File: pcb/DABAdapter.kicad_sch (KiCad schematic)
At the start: 39 parts, among them J1 RFShield_OnePiece, J2 Ant, J3 Conn_01x06, J4 AudioJack3_Ground, J6 Conn_01x06, U3 abcdefg, U4 MIC5504-1.8YM5, Y1 19.2Mhz

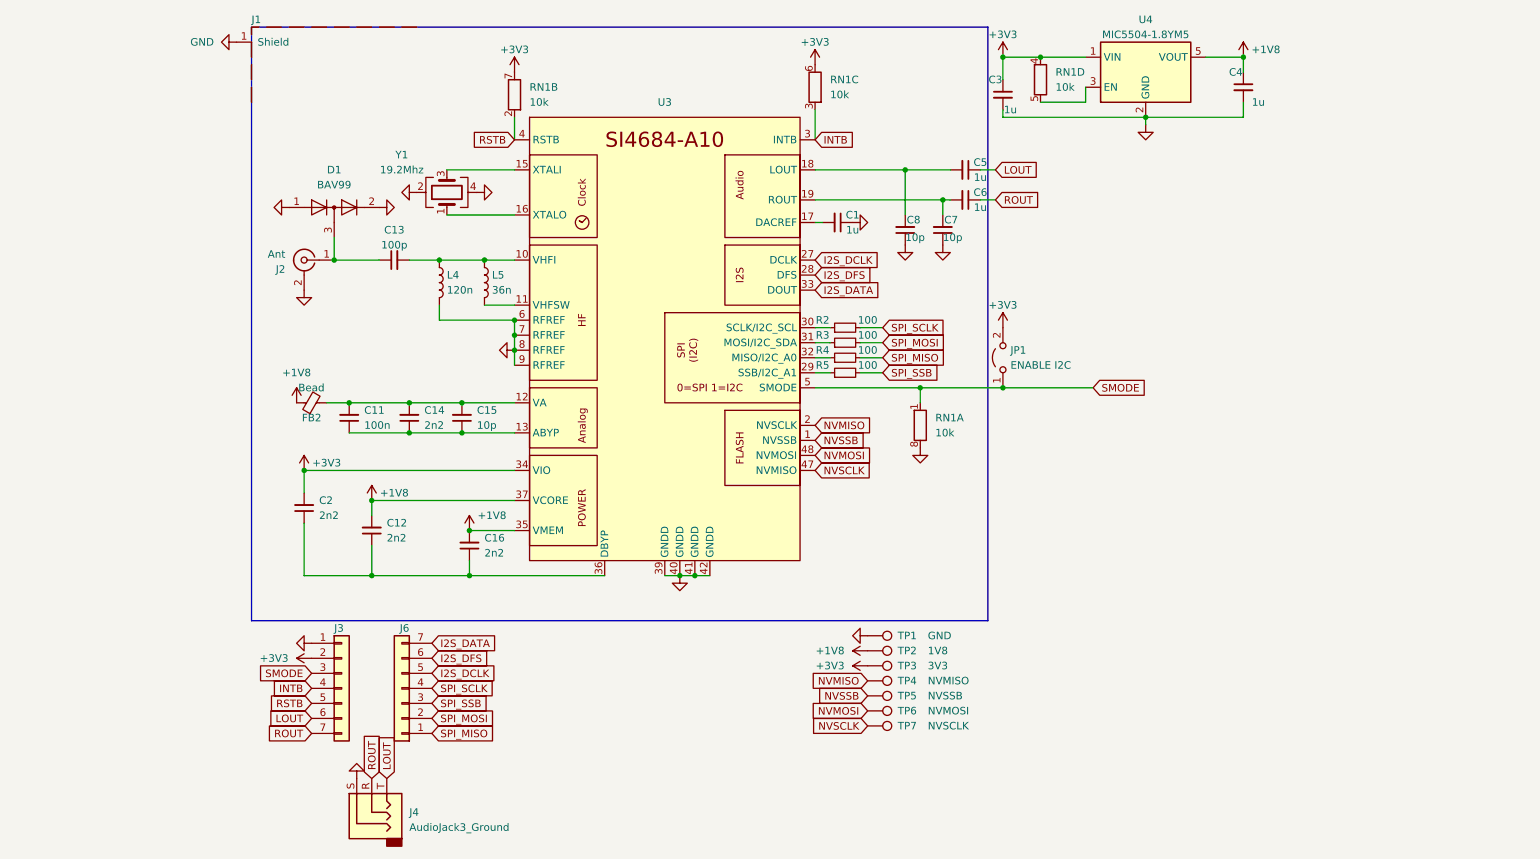
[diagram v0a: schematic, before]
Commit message: Add flash chip to the layout
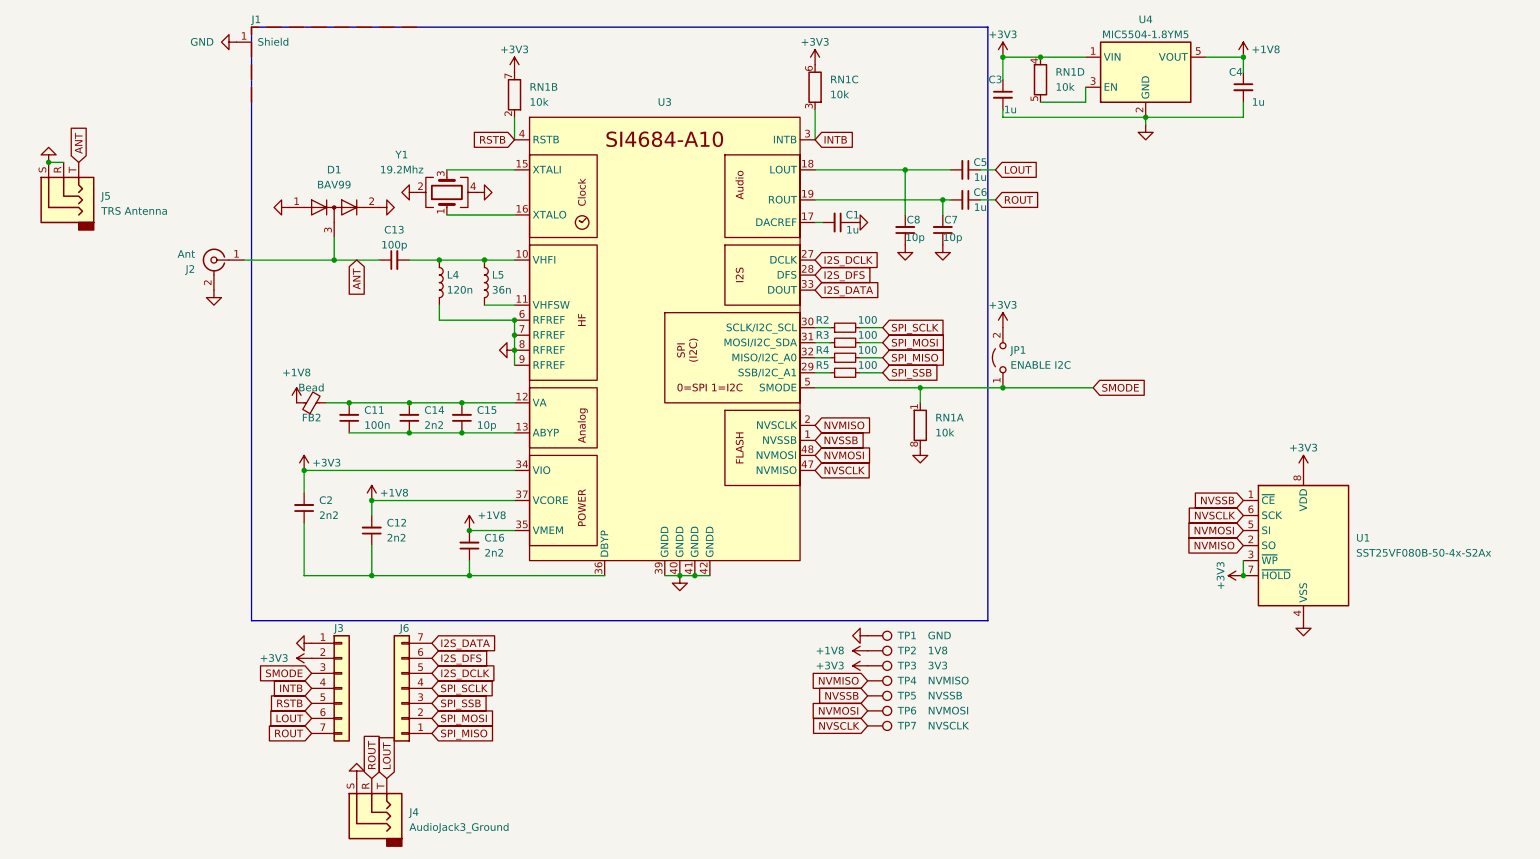
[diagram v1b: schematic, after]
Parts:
- added J5: TRS Antenna, Connector_Audio:Jack_3.5mm_CUI_SJ-3523-SMT_Horizontal, symbol Connector_Audio:AudioJack3
- added U1: SST25VF080B-50-4x-S2Ax, Package_SO:SOIC-8_5.275x5.275mm_P1.27mm, symbol Memory_Flash:SST25VF080B-50-4x-S2Ax
- C15, C7, C8: footprint jlc_footprints:C0603 -> jlc_footprints:C0402
- U3: LCSC (none) -> C2654613
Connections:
- net +3V3: now also U1.3 (~{WP}), U1.7 (~{HOLD}), U1.8 (VDD)
- net GND: now also J5.R, J5.S, U1.4 (VSS)
- net NVMISO: now also U1.2 (SO)
- net NVMOSI: now also U1.5 (SI)
- net NVSCLK: now also U1.6 (SCK)
- net NVSSB: now also U1.1 (~{CE})
- net ANT: now reaches C13.1, D1.3 (K), J2.1 (In)
- net ANT: now also J5.T
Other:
- moved on the sheet: J2

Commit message: Routing of the pcb
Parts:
- removed J5: TRS Antenna, Connector_Audio:Jack_3.5mm_CUI_SJ-3523-SMT_Horizontal, symbol Connector_Audio:AudioJack3
- removed JP1: ENABLE I2C, symbol Jumper:Jumper_2_Open
- removed RN1: 10k, jlc_footprints:RES-ARRAY-SMD_0603-8P-L3.2-W1.6-BL, symbol Device:R_Network04_Split
- added R1, R6, R7, R8: 10k, jlc_footprints:C0402, symbol Device:R_Small
- U1: now not fitted
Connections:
- net +3V3: now also R1.1, R6.1, R7.1
- net GND: now also R8.2
- net I2S_DCLK: now also J6.6 (Pin_6); no longer J6.5 (Pin_5)
- net I2S_DFS: now also J6.5 (Pin_5); no longer J6.6 (Pin_6)
- net INTB: now also J3.5 (Pin_5), R6.2; no longer J3.4 (Pin_4)
- net LOUT: now also J3.4 (Pin_4); no longer J3.6 (Pin_6)
- net ROUT: now also J3.3 (Pin_3); no longer J3.7 (Pin_7)
- net RSTB: now also J3.6 (Pin_6), R7.2; no longer J3.5 (Pin_5)
- net SMODE: now also J3.7 (Pin_7), R8.1; no longer J3.3 (Pin_3)
- net SPI_SCLK: now also J6.3 (Pin_3); no longer J6.4 (Pin_4)
- net SPI_SSB: now also J6.4 (Pin_4); no longer J6.3 (Pin_3)
- net at U4.3 (EN): now also R1.2
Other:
- moved on the sheet: C3, C4, J6, R2, R3, R4, R5, U4

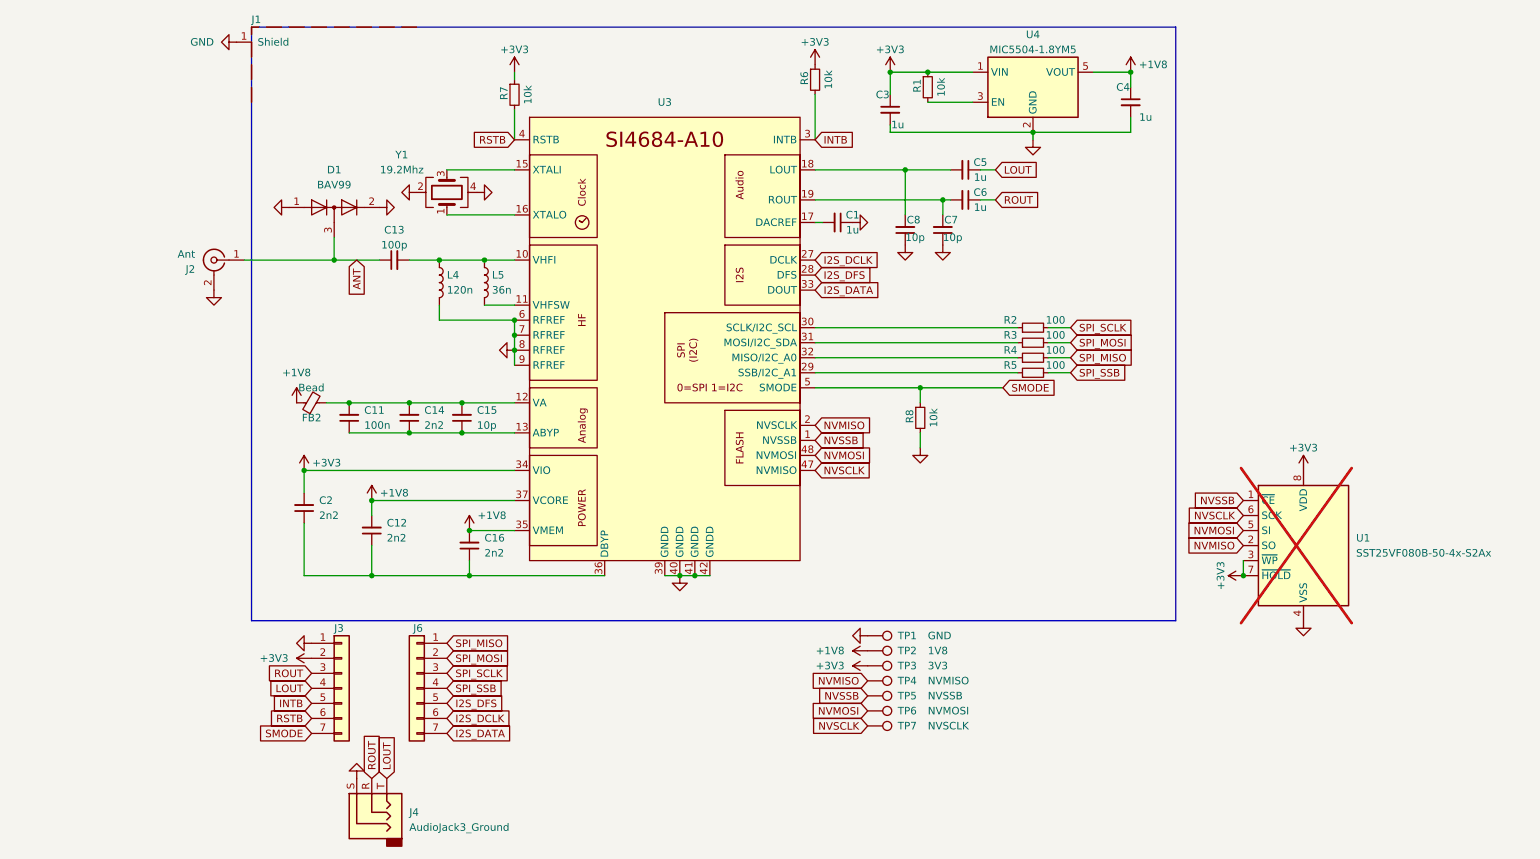
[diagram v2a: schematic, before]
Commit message: DRC and add step file of QFN package
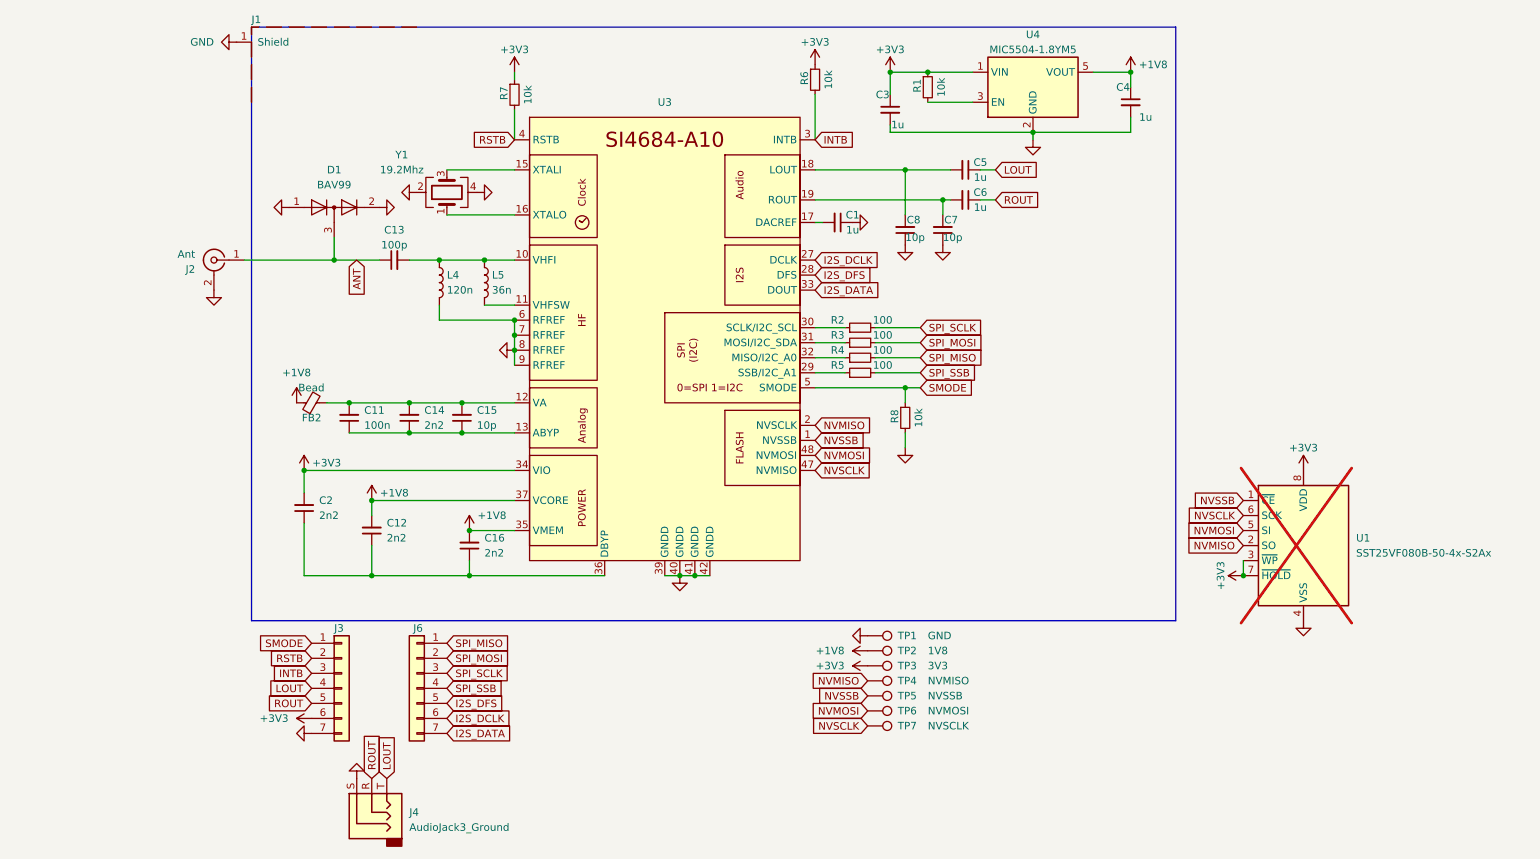
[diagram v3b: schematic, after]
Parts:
- J4: footprint Connector_Audio:Jack_3.5mm_CUI_SJ-3523-SMT_Horizontal -> Connector_Audio:Jack_3.5mm_CUI_SJ-3524-SMT_Horizontal
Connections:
- net +3V3: now also J3.6 (Pin_6); no longer J3.2 (Pin_2)
- net GND: now also J3.7 (Pin_7); no longer J3.1 (Pin_1)
- net INTB: now also J3.3 (Pin_3); no longer J3.5 (Pin_5)
- net ROUT: now also J3.5 (Pin_5); no longer J3.3 (Pin_3)
- net RSTB: now also J3.2 (Pin_2); no longer J3.6 (Pin_6)
- net SMODE: now also J3.1 (Pin_1); no longer J3.7 (Pin_7)
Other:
- moved on the sheet: R2, R3, R4, R5, R8

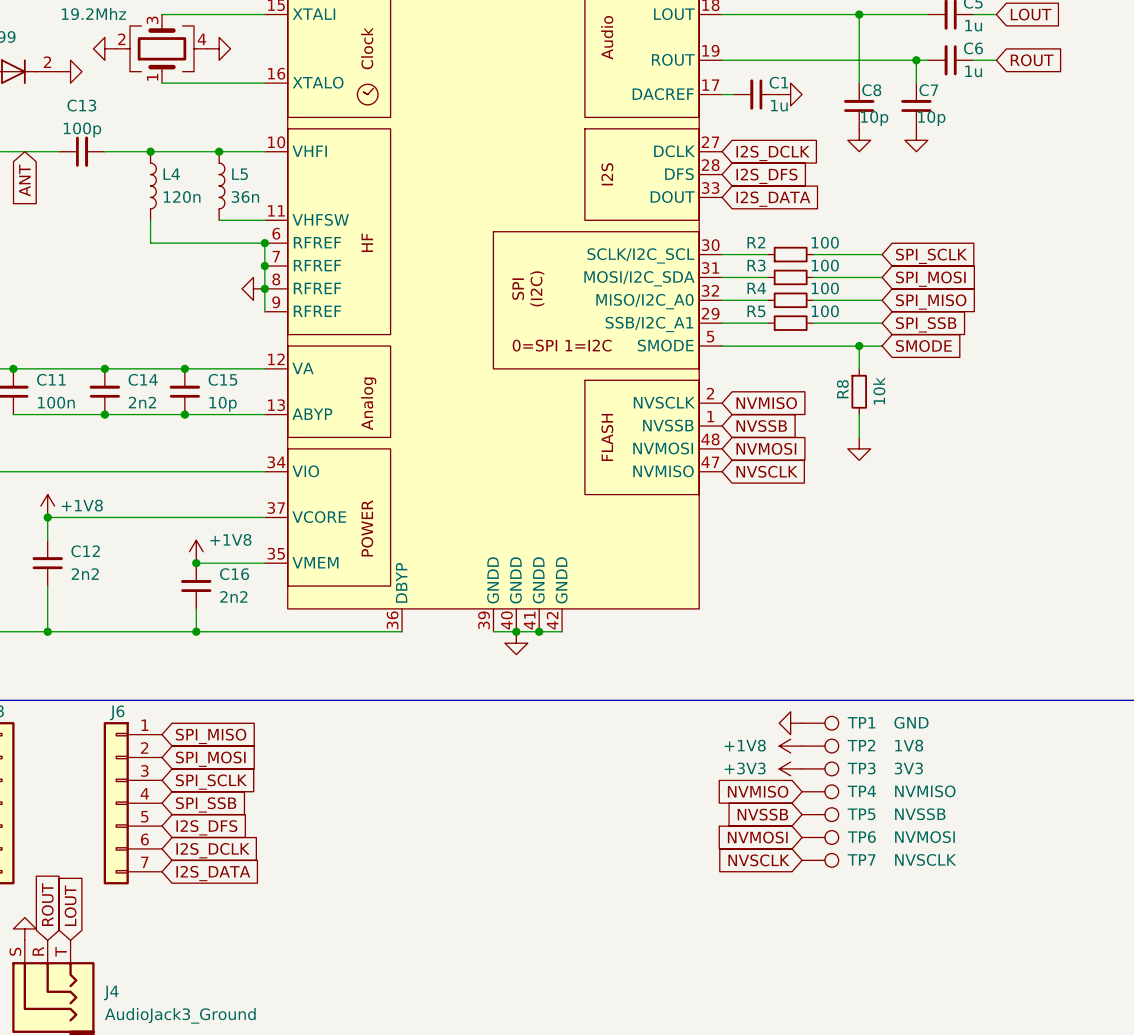
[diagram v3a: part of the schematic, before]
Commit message: Rename FS to RLCLK
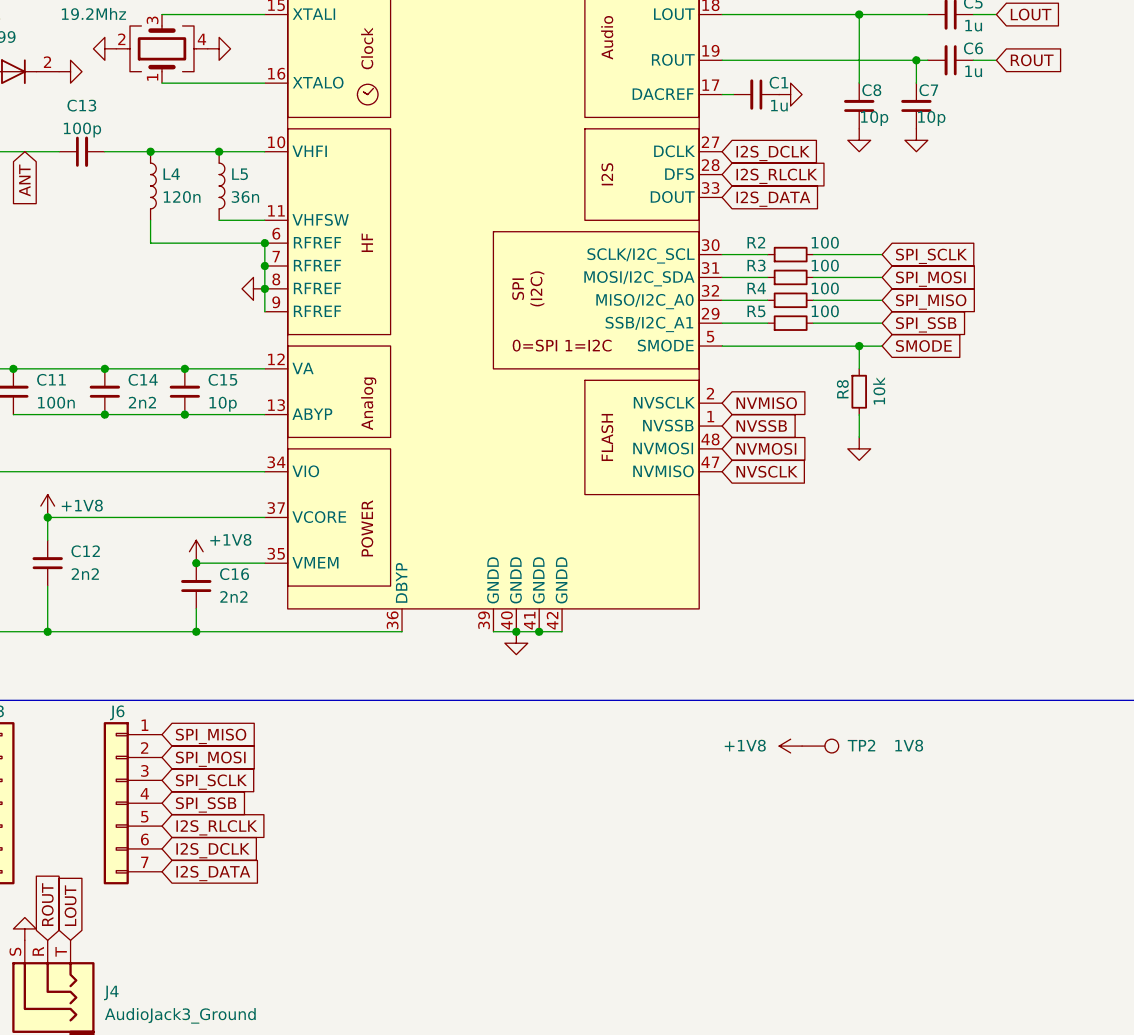
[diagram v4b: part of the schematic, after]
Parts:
- removed TP1: GND, symbol Connector:TestPoint
- removed TP3: 3V3, symbol Connector:TestPoint
- removed TP4: NVMISO, symbol Connector:TestPoint
- removed TP5: NVSSB, symbol Connector:TestPoint
- removed TP6: NVMOSI, symbol Connector:TestPoint
- removed TP7: NVSCLK, symbol Connector:TestPoint
- TP2: footprint (none) -> TestPoint:TestPoint_Pad_D1.0mm
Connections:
- net I2S_DFS renamed I2S_RLCLK
